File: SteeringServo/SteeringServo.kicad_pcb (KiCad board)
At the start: 2 copper layers, 78.1 x 47 mm, 10 parts, among them J1 MotorConnector, J2 To 12V Converter, J3 Signal, SW1 SW_Push, U1 TLE5205, U2 StatusLED

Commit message: pcb for servo
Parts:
- D1: footprint Diode_THT:D_A-405_P7.62mm_Horizontal -> Diode_THT:D_A-405_P10.16mm_Horizontal
- J2: footprint Connector_Phoenix_MSTB:PhoenixContact_MSTBVA_2,5_3-G-5,08_1x03_P5.08mm_Vertical -> Connector_Phoenix_MSTB:PhoenixContact_MSTBVA_2,5_2-G-5,08_1x02_P5.08mm_Vertical
- U1, U2: moved to B.Cu
- moved J2 32.4 mm to (167.0, 31.1), turned to 270 degrees
- moved C1 31.0 mm to (207.6, 34.3), turned to 90 degrees
- moved J1 19.1 mm to (185.4, 62.9), turned to 180 degrees
- moved C2 11.7 mm to (177.2, 35.6), turned to 90 degrees
- moved J3 8.84 mm to (220.3, 34.3), turned to 90 degrees
- moved D1 7.24 mm to (188.0, 40.6)
- moved U2 2.62 mm to (230.5, 63.5), turned to 180 degrees
- moved SW1 2.29 mm to (225.4, 64.1)
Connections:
- J1 pad 1: M! -> M1
- J1 pad 2: GND -> 5V
- J1 pad 4: 5V -> GND
- J2 pad 2: VIN -> 12V
- U1 pad 3: M_IN1 -> M_IN_1
- U2 pad 5: Net-(U2-Pad5) -> (no net)
- U2 pad 6: Net-(U2-Pad6) -> (no net)
- XA1 pad 3V3: Net-(XA1-Pad3V3) -> (no net)
- XA1 pad A0: SERVO_POTI -> (no net)
- XA1 pad A1: Net-(XA1-PadA1) -> (no net)
- XA1 pad A2: Net-(XA1-PadA2) -> (no net)
- XA1 pad A3: Net-(XA1-PadA3) -> (no net)
- XA1 pad A6: Net-(XA1-PadA6) -> SERVO_POTI
- XA1 pad A7: Net-(XA1-PadA7) -> (no net)
- XA1 pad AREF: Net-(XA1-PadAREF) -> (no net)
- XA1 pad D0: Net-(XA1-PadD0) -> (no net)
- XA1 pad D1: Net-(XA1-PadD1) -> (no net)
- XA1 pad D10: M_IN_1 -> (no net)
- XA1 pad D11: M_IN_2 -> (no net)
- XA1 pad D12: M_ERR -> Calibrate
- XA1 pad D13: Net-(XA1-PadD13) -> (no net)
- XA1 pad D2: Net-(XA1-PadD2) -> (no net)
- XA1 pad D3: Net-(XA1-PadD3) -> (no net)
- XA1 pad D6: M_ERR -> M_IN_2
- XA1 pad D7: Calibrate -> M_IN_1
- XA1 pad D8: Net-(XA1-PadD8) -> M_ERR
- XA1 pad D9: Signal -> (no net)
- XA1 pad RST1: Net-(XA1-PadRST1) -> (no net)
- XA1 pad RST2: Net-(XA1-PadRST2) -> (no net)
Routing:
- net 5V: track 0.00 -> 102.8 mm, vias 0 -> 2
- net GND: track 161.3 -> 236.1 mm
- net M_ERR: track 0.00 -> 53.9 mm
- net M_IN_1: track 0.00 -> 50.0 mm
- net M_IN_2: track 0.00 -> 44.4 mm
- net (no net): track 0.00 -> 43.1 mm
- net SERVO_POTI: track 25.6 -> 65.6 mm, vias 0 -> 2
- net M1: track 0.00 -> 38.3 mm, vias 0 -> 2
- net LED_DIN: track 0.00 -> 35.5 mm
- net LED_CIN: track 0.00 -> 30.7 mm
- net M2: track 0.00 -> 21.3 mm
- net Net-(D1-Pad2): track 0.00 -> 12.5 mm
- net SDA: track 22.9 -> 13.1 mm
- net 12V: track 33.3 -> 43.0 mm
- net SCL: track 22.5 -> 17.5 mm
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- added copper zone on B.Cu, net GND

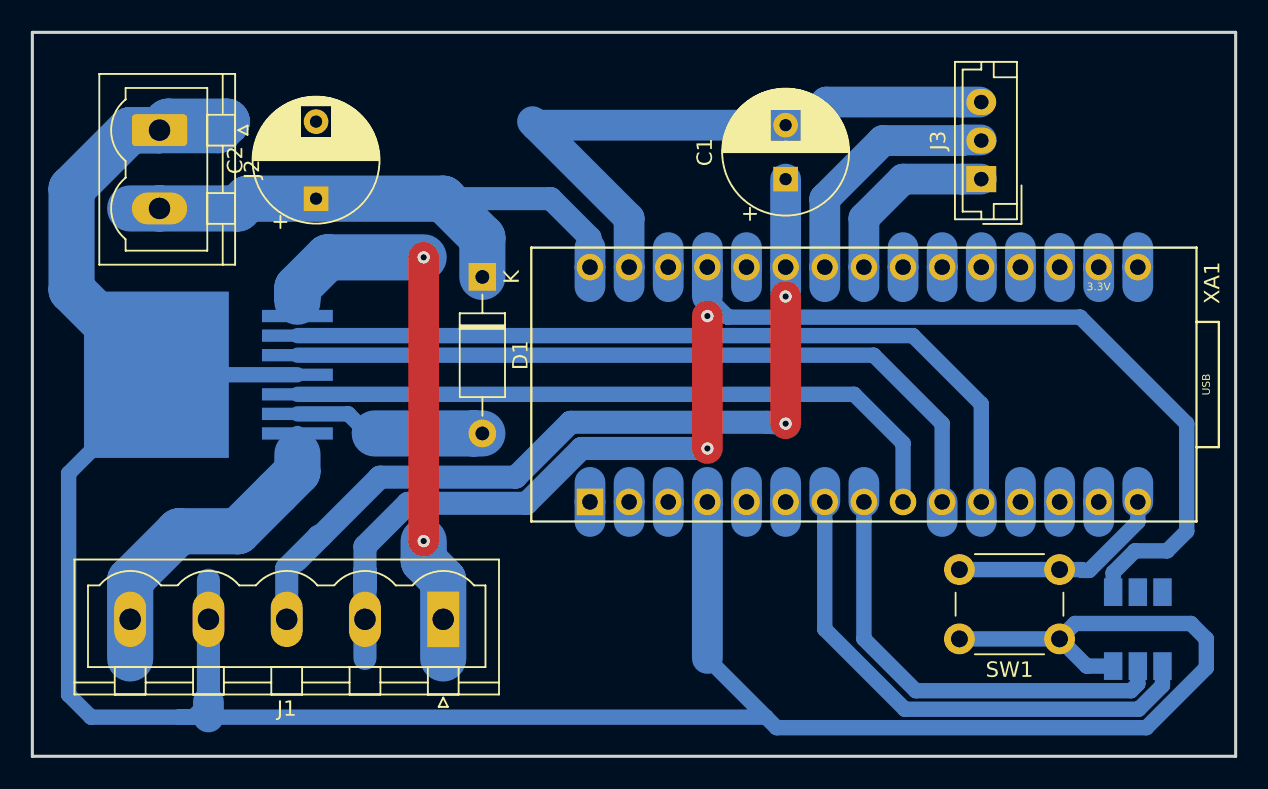
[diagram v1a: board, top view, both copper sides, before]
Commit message: readded legacy servo support
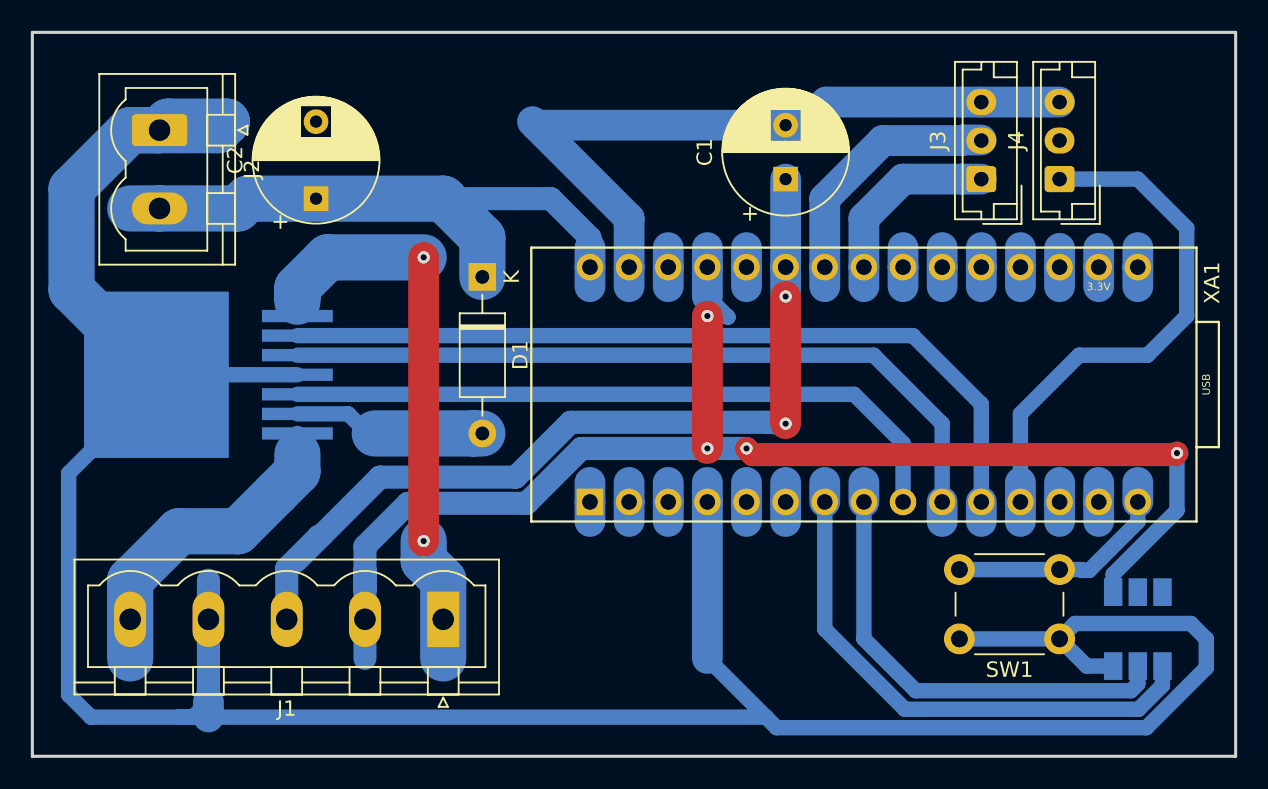
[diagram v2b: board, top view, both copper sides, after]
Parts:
- added J4: Signal, Connector_JST:JST_EH_B3B-EH-A_1x03_P2.50mm_Vertical, F.Cu at (225.4, 34.3)
- J3: footprint Connector_JST:JST_EH_B03B-EH-A_1x03_P2.50mm_Vertical -> Connector_JST:JST_EH_B3B-EH-A_1x03_P2.50mm_Vertical
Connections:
- XA1 pad D9: (no net) -> Signal
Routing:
- net Signal: track 0.00 -> 37.0 mm
- net 5V: track 102.8 -> 97.5 mm, vias 2 -> 4
- net GND: track 236.1 -> 241.2 mm
- net (no net): track 43.1 -> 40.5 mm

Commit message: improved layout
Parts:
- moved U2 9.61 mm to (221.0, 62.2), turned to 90 degrees
- moved SW1 3.70 mm to (228.6, 66.0), turned to 90 degrees
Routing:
- net GND: track 241.2 -> 185.4 mm
- net LED_DIN: track 35.5 -> 15.6 mm
- net LED_CIN: track 30.7 -> 13.1 mm
- net SERVO_POTI: track 65.6 -> 79.6 mm
- net 5V: track 97.5 -> 107.8 mm
- net M_ERR: track 53.9 -> 51.5 mm
- net Calibrate: track 15.5 -> 13.1 mm
- net M_IN_1: track 50.0 -> 48.2 mm
- net Signal: track 37.0 -> 38.1 mm

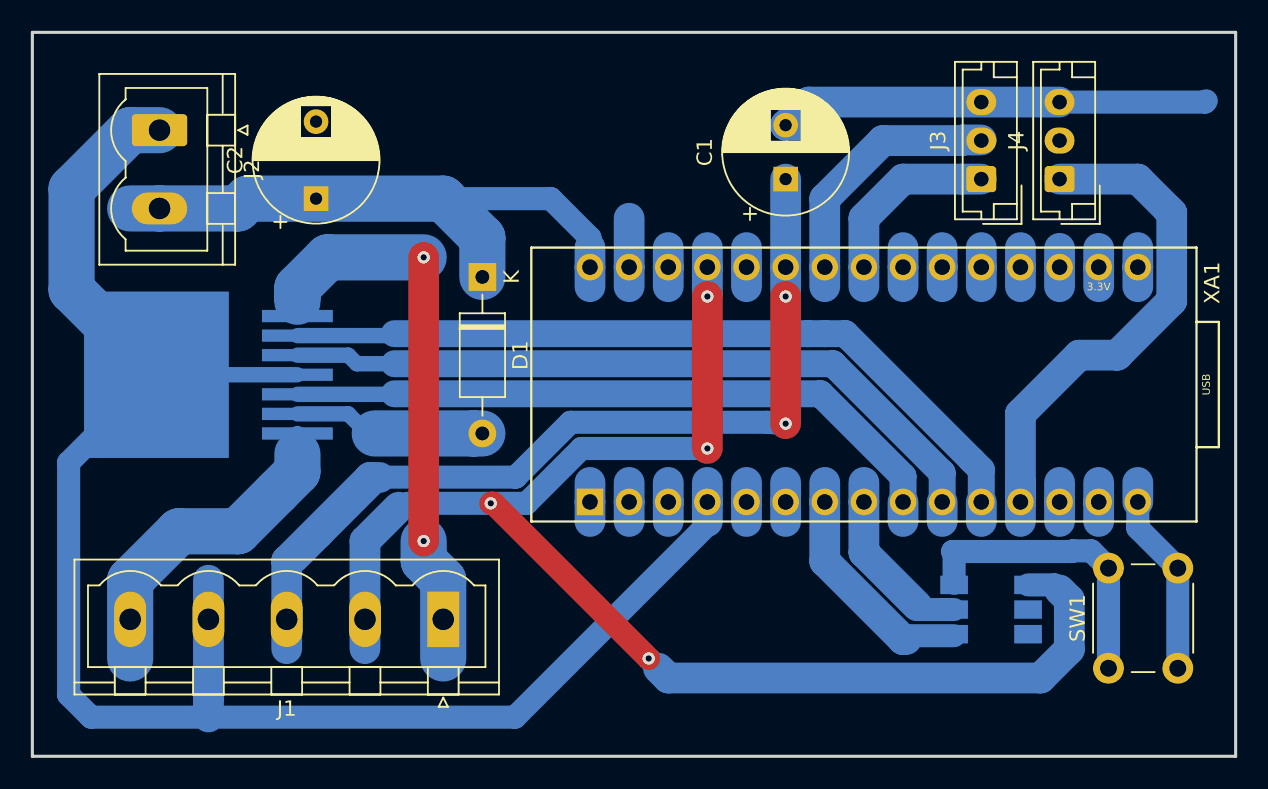
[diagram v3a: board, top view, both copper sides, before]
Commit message: prevent nano from buring the am1117 when being powered by usb
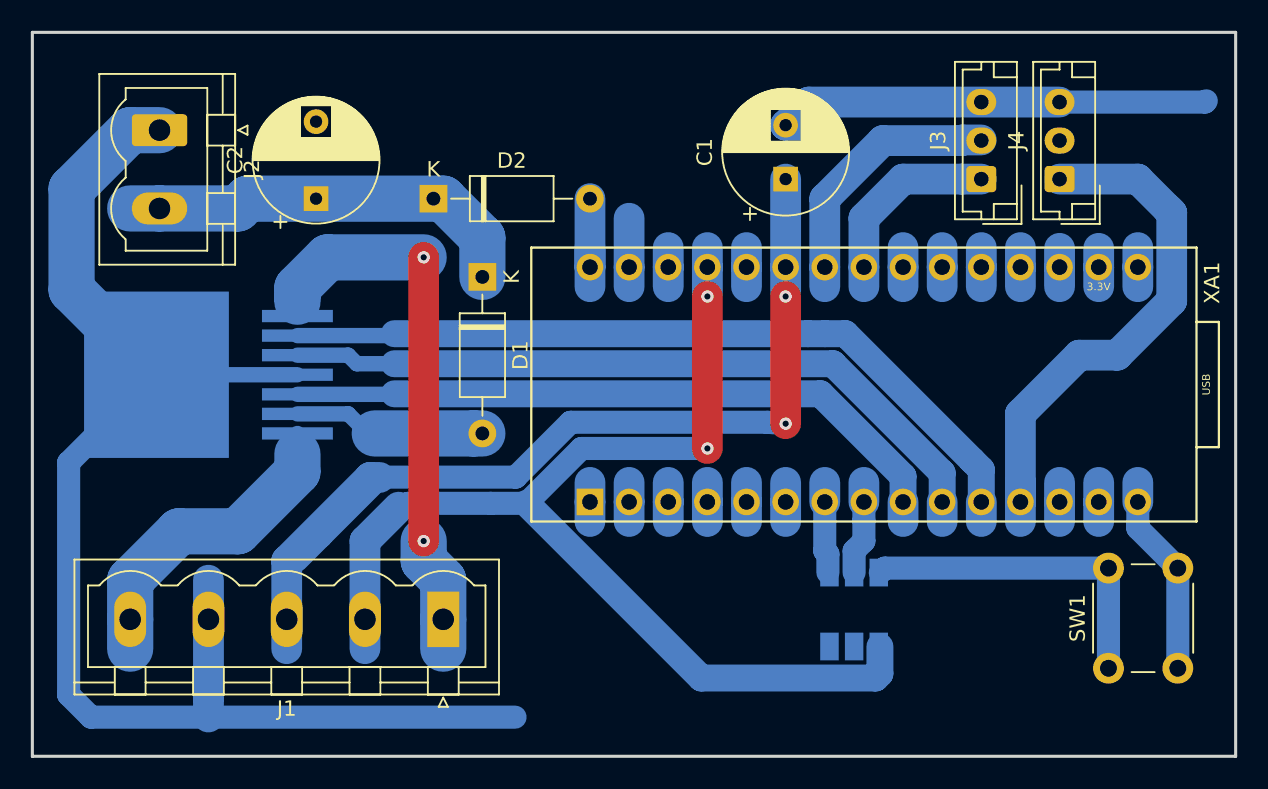
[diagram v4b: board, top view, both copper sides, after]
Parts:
- added D2: DIODE, Diode_THT:D_A-405_P10.16mm_Horizontal, F.Cu at (184.8, 35.6)
- moved U2 8.89 mm to (212.1, 62.2), turned to 0 degrees
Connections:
- J4 pad 2: (no net) -> Net-(J4-Pad2)
- U2 pad 5: (no net) -> Net-(U2-Pad5)
- U2 pad 6: (no net) -> Net-(U2-Pad6)
- XA1 pad 3V3: (no net) -> Net-(XA1-Pad3V3)
- XA1 pad A0: (no net) -> Net-(XA1-PadA0)
- XA1 pad A1: (no net) -> Net-(XA1-PadA1)
- XA1 pad A2: (no net) -> Net-(XA1-PadA2)
- XA1 pad A3: (no net) -> Net-(XA1-PadA3)
- XA1 pad A7: (no net) -> Net-(XA1-PadA7)
- XA1 pad AREF: (no net) -> Net-(XA1-PadAREF)
- XA1 pad D0: (no net) -> Net-(XA1-PadD0)
- XA1 pad D1: (no net) -> Net-(XA1-PadD1)
- XA1 pad D10: (no net) -> Net-(XA1-PadD10)
- XA1 pad D11: (no net) -> Net-(XA1-PadD11)
- XA1 pad D13: (no net) -> Net-(XA1-PadD13)
- XA1 pad D2: (no net) -> Net-(XA1-PadD2)
- XA1 pad D3: (no net) -> Net-(XA1-PadD3)
- XA1 pad GND1: GND -> Net-(XA1-PadGND1)
- XA1 pad RST1: (no net) -> Net-(XA1-PadRST1)
- XA1 pad RST2: (no net) -> Net-(XA1-PadRST2)
- XA1 pad VIN: 12V -> Net-(D2-Pad2)
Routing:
- net (no net): track 40.5 -> 0.00 mm
- net 5V: track 107.8 -> 88.0 mm, vias 4 -> 2
- net GND: track 185.4 -> 165.9 mm
- net 12V: track 43.0 -> 26.7 mm
- net LED_DIN: track 15.6 -> 5.94 mm
- net Net-(D2-Pad2): track 0.00 -> 8.21 mm
- net LED_CIN: track 13.1 -> 6.12 mm
- net Net-(XA1-PadGND1): track 0.00 -> 4.03 mm
- net Net-(XA1-PadRST2): track 0.00 -> 2.54 mm
- net Net-(XA1-PadRST1): track 0.00 -> 2.54 mm
- net Net-(XA1-PadD3): track 0.00 -> 2.54 mm
- net Net-(XA1-PadD2): track 0.00 -> 2.54 mm
- net Net-(XA1-PadD13): track 0.00 -> 2.54 mm
- net Net-(XA1-PadD11): track 0.00 -> 2.54 mm
- net Net-(XA1-PadD10): track 0.00 -> 2.54 mm
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
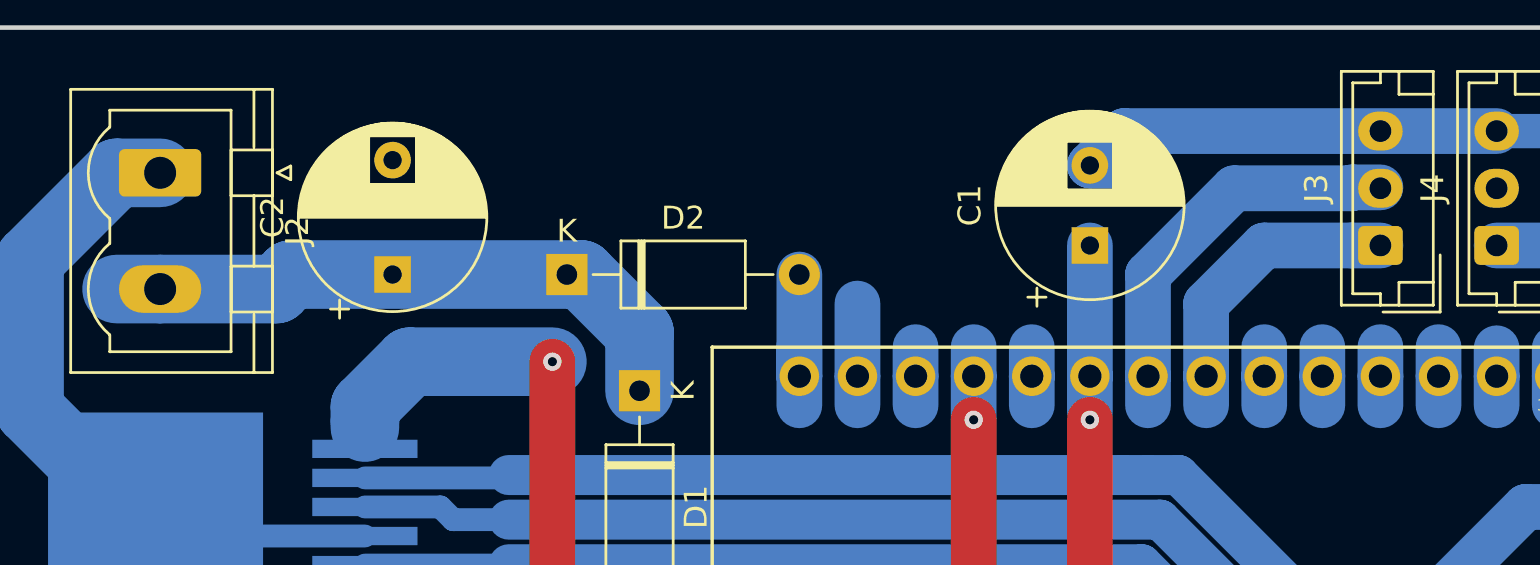
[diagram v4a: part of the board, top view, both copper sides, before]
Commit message: fixed multiple issues with servocontroller
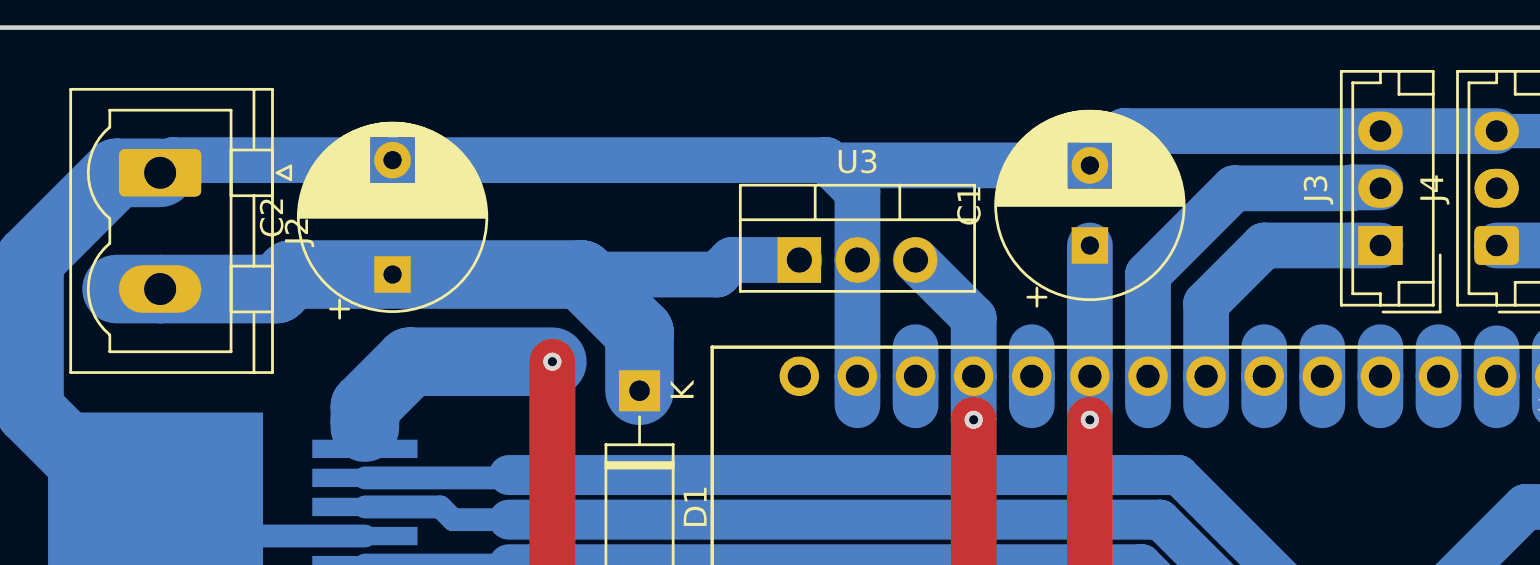
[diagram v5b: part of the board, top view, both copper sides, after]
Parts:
- removed D2: DIODE, Diode_THT:D_A-405_P10.16mm_Horizontal
- added U3: L7805, Package_TO_SOT_THT:TO-220-3_Vertical, F.Cu at (194.9, 34.9)
- J3: footprint Connector_JST:JST_EH_B3B-EH-A_1x03_P2.50mm_Vertical -> Connector_JST:JST_EH_B03B-EH-A_1x03_P2.50mm_Vertical
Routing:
- net GND: track 165.9 -> 213.7 mm
- net 12V: track 26.7 -> 36.5 mm
- net Net-(XA1-PadVIN): track 8.21 -> 0.00 mm
- net 5V: track 88.0 -> 92.8 mm
